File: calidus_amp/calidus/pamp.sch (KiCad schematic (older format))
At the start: 50 parts, among them U6 TDA7293, U7 TDA7293

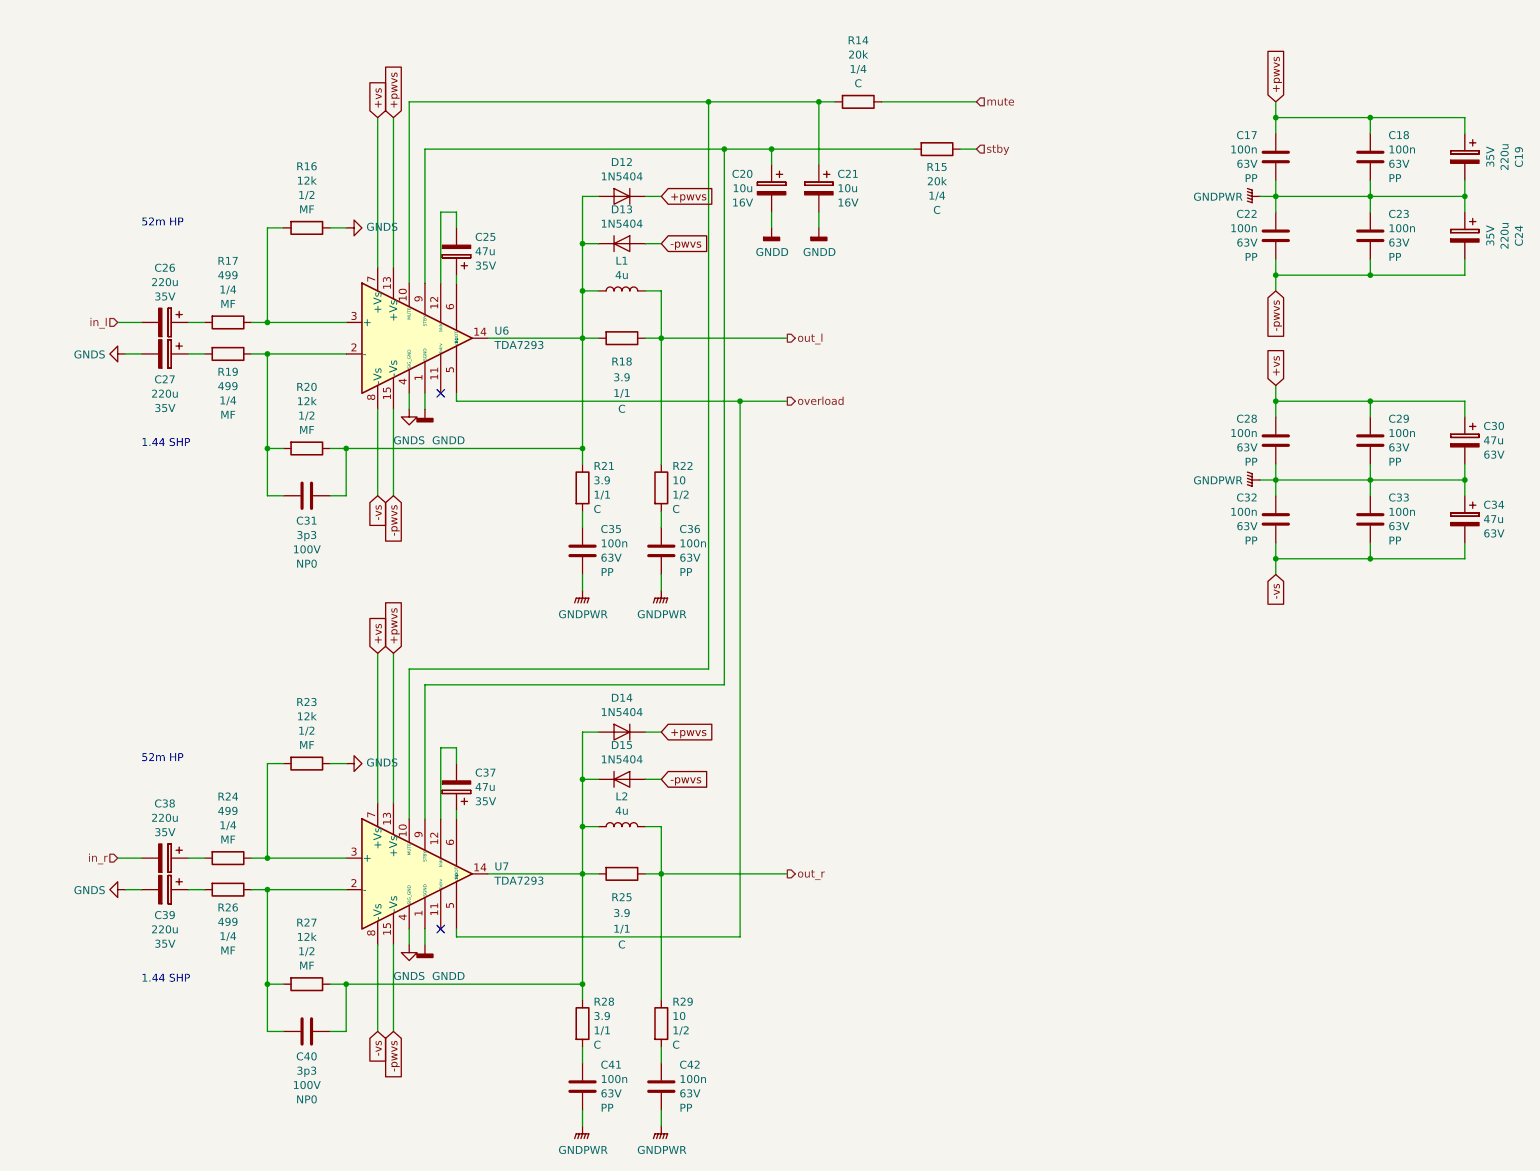
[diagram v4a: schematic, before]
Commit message: Updated schematic and footprinted Rybicon capacitors
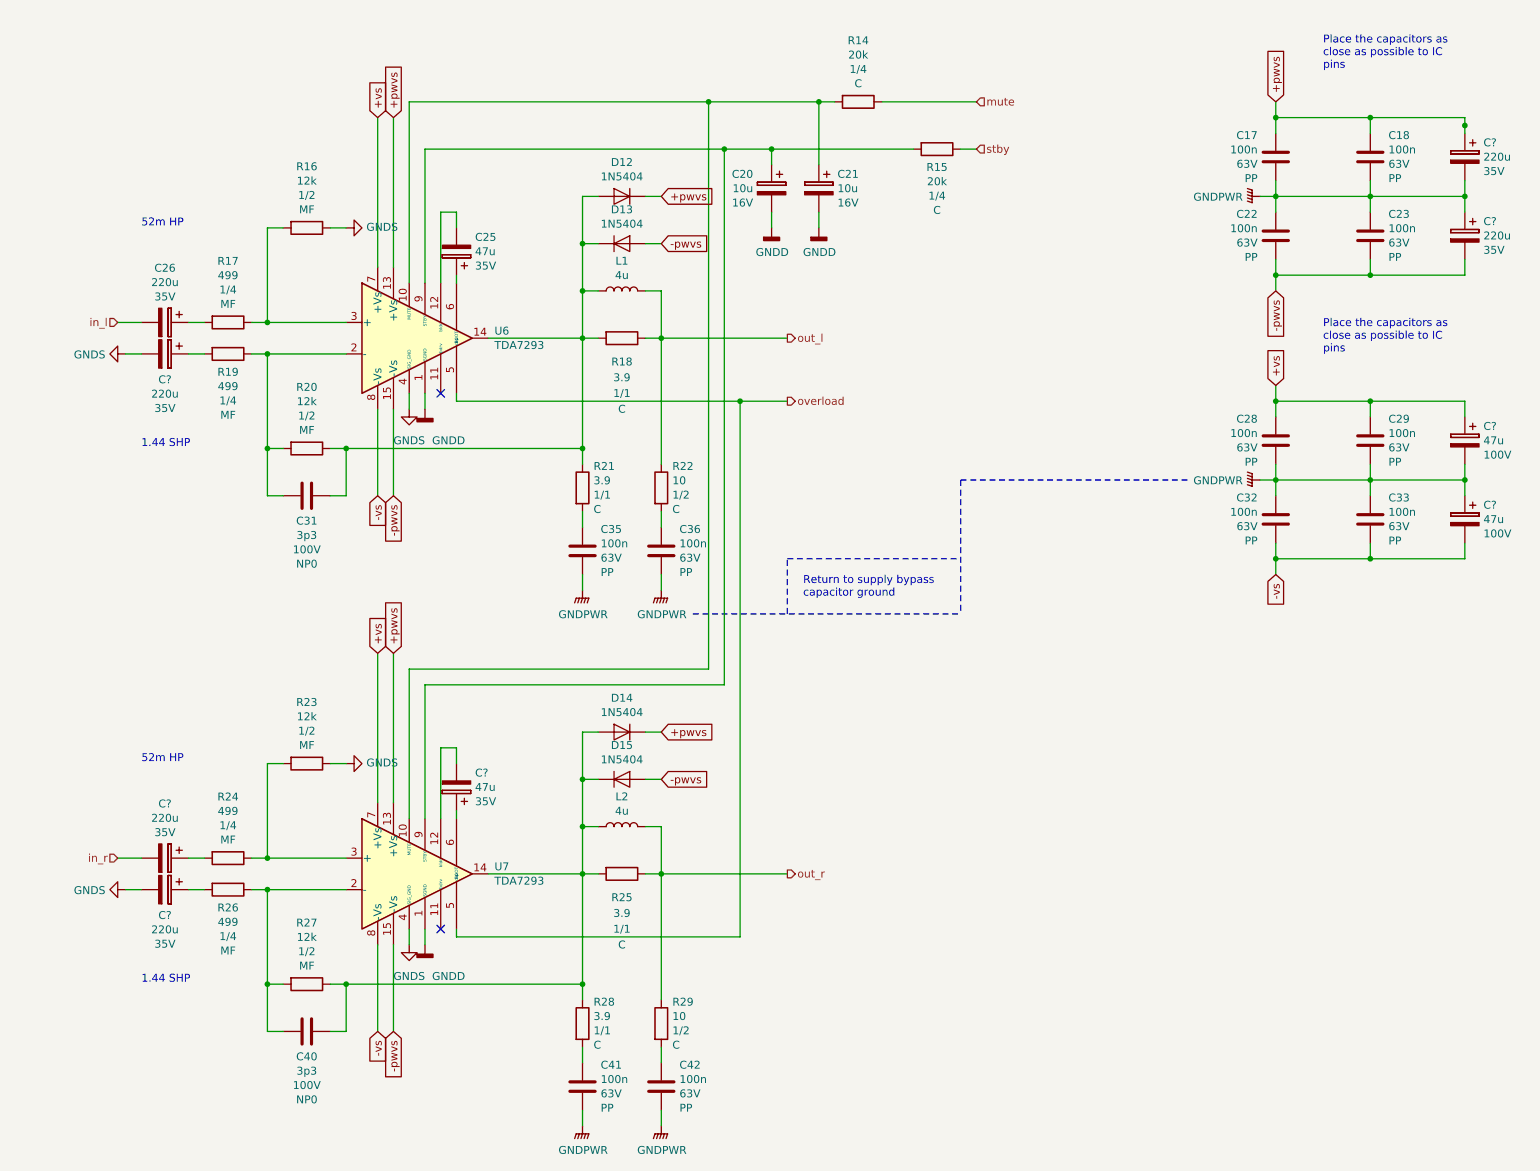
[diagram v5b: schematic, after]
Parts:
- removed C19, C24, C27, C38, C39: 220u, symbol Device:CP
- removed C30, C34, C37: 47u, symbol Device:CP
- added C?: 47u, Capacitor_THT:CP_Radial_D6.3mm_P2.50mm, symbol Device:CP
- added C? (x2): 47u, Capacitor_THT:CP_Radial_D10.0mm_P5.00mm, symbol Device:CP
- added C? (x5): 220u, Capacitor_THT:CP_Radial_D10.0mm_P5.00mm, symbol Device:CP
- C25: footprint (none) -> Capacitor_THT:CP_Radial_D6.3mm_P2.50mm; Manufacturer (none) -> Rybicon:35YXF47MEFC6.3X11; Supplier1 (none) -> Farnell:1144626
- C26: footprint (none) -> Capacitor_THT:CP_Radial_D10.0mm_P5.00mm; Manufacturer (none) -> Rybicon:35YXF220MEFC10X12.5; Supplier1 (none) -> Farnel:1144628
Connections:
- net +pwvs: now also C?.1
- net +vs: now also C?.1
- net -pwvs: now also C?.2
- net -vs: now also C?.2
- net GNDPWR: now also C?.1, C?.1, C?.2, C?.2
- net GNDS: now also C?.2, C?.2
- net in_r: now also C?.2
- net at U7.12 (bldr): now also C?.2
- net at U7.6 (BOOT): now also C?.1
- net at R19.2: now also C?.1
- net at R26.2: now also C?.1
- net at R24.2: now also C?.1
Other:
- note added: "Place the capacitors as\nclose as possible to IC\npins"
- note added: "Return to supply bypass \ncapacitor ground"
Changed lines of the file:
@@
 F 0 "C26" V 1905 2400 50  0000 C CNN
 F 1 "220u" V 1996 2400 50  0000 C CNN
-F 2 "" H 2288 2250 50  0001 C CNN
-F 3 "~" H 2250 2400 50  0001 C CNN
+F 2 "Capacitor_THT:CP_Radial_D10.0mm_P5.00mm" H 2288 2250 50  0001 C CNN
+F 3 "http://www.farnell.com/datasheets/2321304.pdf" H 2250 2400 50  0001 C CNN
 F 4 "35V" V 2087 2400 50  0000 C CNN "Voltage"
+F 5 "Rybicon:35YXF220MEFC10X12.5" V 2250 2400 50  0001 C CNN "Manufacturer"
+F 6 "Farnel:1144628" V 2250 2400 50  0001 C CNN "Supplier1"
 	1    2250 2400
 	0    1    1    0
@@
 F 0 "C25" H 3982 1859 50  0000 R CNN
 F 1 "47u" H 3982 1950 50  0000 R CNN
-F 2 "" H 4138 1800 50  0001 C CNN
-F 3 "~" H 4100 1950 50  0001 C CNN
+F 2 "Capacitor_THT:CP_Radial_D6.3mm_P2.50mm" H 4138 1800 50  0001 C CNN
+F 3 "http://www.farnell.com/datasheets/2321304.pdf" H 4100 1950 50  0001 C CNN
 F 4 "35V" H 3982 2041 50  0000 R CNN "Voltage"
+F 5 "Rybicon:35YXF47MEFC6.3X11" H 4100 1950 50  0001 C CNN "Manufacturer"
+F 6 "Farnell:1144626" H 4100 1950 50  0001 C CNN "Supplier1"
 	1    4100 1950
 	-1   0    0    1
@@
 $EndComp
 $Comp
-L Device:CP C27
-U 1 1 5C4684D2
-P 2250 2600
-F 0 "C27" V 2413 2600 50  0000 C CNN
-F 1 "220u" V 2504 2600 50  0000 C CNN
-F 2 "" H 2288 2450 50  0001 C CNN
-F 3 "~" H 2250 2600 50  0001 C CNN
-F 4 "35V" V 2595 2600 50  0000 C CNN "Voltage"
-	1    2250 2600
-	0    1    1    0
-$EndComp
-$Comp
-L Device:CP C39
-U 1 1 5C468E95
-P 2250 6000
-F 0 "C39" V 2413 6000 50  0000 C CNN
-F 1 "220u" V 2504 6000 50  0000 C CNN
-F 2 "" H 2288 5850 50  0001 C CNN
-F 3 "~" H 2250 6000 50  0001 C CNN
-F 4 "35V" V 2595 6000 50  0000 C CNN "Voltage"
-	1    2250 6000
-	0    1    1    0
-$EndComp
-$Comp
-L Device:CP C38
-U 1 1 5C468F39
-P 2250 5800
-F 0 "C38" V 1905 5800 50  0000 C CNN
-F 1 "220u" V 1996 5800 50  0000 C CNN
-F 2 "" H 2288 5650 50  0001 C CNN
-F 3 "~" H 2250 5800 50  0001 C CNN
-F 4 "35V" V 2087 5800 50  0000 C CNN "Voltage"
-	1    2250 5800
-	0    1    1    0
-$EndComp
-$Comp
 L Device:R R16
 U 1 1 5C469739
@@
 $EndComp
 $Comp
-L Device:CP C37
-U 1 1 5C469AA7
-P 4100 5350
-F 0 "C37" H 3982 5259 50  0000 R CNN
-F 1 "47u" H 3982 5350 50  0000 R CNN
-F 2 "" H 4138 5200 50  0001 C CNN
-F 3 "~" H 4100 5350 50  0001 C CNN
-F 4 "35V" H 3982 5441 50  0000 R CNN "Voltage"
-	1    4100 5350
-	-1   0    0    1
-$EndComp
-$Comp
 L Device:CP C21
 U 1 1 5C46A2D8
@@
 Wire Wire Line
 	9200 1600 9300 1600
-$Comp
-L Device:CP C19
-U 1 1 5C5797F2
-P 10500 1350
-F 0 "C19" V 10155 1350 50  0000 C CNN
-F 1 "220u" V 10246 1350 50  0000 C CNN
-F 2 "" H 10538 1200 50  0001 C CNN
-F 3 "~" H 10500 1350 50  0001 C CNN
-F 4 "35V" V 10337 1350 50  0000 C CNN "Voltage"
-	1    10500 1350
-	-1   0    0    -1
-$EndComp
-Wire Wire Line
-	10500 1200 10500 1100
+Wire Wire Line
+	10500 1200 10500 1150
 Wire Wire Line
 	9300 1100 9900 1100
@@
 Connection ~ 9900 2100
 Connection ~ 10500 1600
-$Comp
-L Device:CP C24
-U 1 1 5C59B1CB
-P 10500 1850
-F 0 "C24" V 10155 1850 50  0000 C CNN
-F 1 "220u" V 10246 1850 50  0000 C CNN
-F 2 "" H 10538 1700 50  0001 C CNN
-F 3 "~" H 10500 1850 50  0001 C CNN
-F 4 "35V" V 10337 1850 50  0000 C CNN "Voltage"
-	1    10500 1850
-	-1   0    0    -1
-$EndComp
 Wire Wire Line
 	10500 1700 10500 1600
@@
 Wire Wire Line
 	10500 3400 10500 3500
-$Comp
-L Device:CP C30
-U 1 1 5C5BB293
+Wire Wire Line
+	10500 3300 10500 3400
+Wire Wire Line
+	10500 3800 10500 3900
+Text Notes 6300 4150 0    50   ~ 0
+Return to supply bypass \ncapacitor ground
+Wire Notes Line
+	6200 3900 7300 3900
+Wire Notes Line
+	6200 4250 6200 3900
+Wire Notes Line
+	5600 4250 7300 4250
+Wire Notes Line
+	7300 3400 8750 3400
+Wire Notes Line
+	7300 3400 7300 4250
+Text Notes 9600 800  0    50   ~ 0
+Place the capacitors as\nclose as possible to IC\npins
+Text Notes 9600 2600 0    50   ~ 0
+Place the capacitors as\nclose as possible to IC\npins
+$Comp
+L Device:CP C?
+U 1 1 5C5AF4B7
+P 4100 5350
+F 0 "C?" H 3982 5259 50  0000 R CNN
+F 1 "47u" H 3982 5350 50  0000 R CNN
+F 2 "Capacitor_THT:CP_Radial_D6.3mm_P2.50mm" H 4138 5200 50  0001 C CNN
+F 3 "http://www.farnell.com/datasheets/2321304.pdf" H 4100 5350 50  0001 C CNN
+F 4 "35V" H 3982 5441 50  0000 R CNN "Voltage"
+F 5 "Rybicon:35YXF47MEFC6.3X11" H 4100 5350 50  0001 C CNN "Manufacturer"
+F 6 "Farnell:1144626" H 4100 5350 50  0001 C CNN "Supplier1"
+	1    4100 5350
+	-1   0    0    1
+$EndComp
+$Comp
+L Device:CP C?
+U 1 1 5C5B3FFC
 P 10500 3150
-F 0 "C30" H 10382 3241 50  0000 R CNN
+AR Path="/5C37BC48/5C5B3FFC" Ref="C?"  Part="1"
+AR Path="/5C37BC7C/5C5B3FFC" Ref="C?"  Part="1"
+F 0 "C?" H 10382 3241 50  0000 R CNN
 F 1 "47u" H 10382 3150 50  0000 R CNN
-F 2 "" H 10538 3000 50  0001 C CNN
-F 3 "~" H 10500 3150 50  0001 C CNN
-F 4 "63V" H 10382 3059 50  0000 R CNN "Voltage"
+F 2 "Capacitor_THT:CP_Radial_D10.0mm_P5.00mm" H 10538 3000 50  0001 C CNN
+F 3 "http://www.farnell.com/datasheets/2124421.pdf" H 10500 3150 50  0001 C CNN
+F 4 "100V" H 10382 3059 50  0000 R CNN "Voltage"
+F 5 "Rybicon:100YXF47MEFC10X16" H 10500 3150 50  0001 C CNN "Manufacturer"
+F 6 "Farnell:1144641" H 10500 3150 50  0001 C CNN "Supplier1"
 	1    10500 3150
 	-1   0    0    -1
 $EndComp
-Wire Wire Line
-	10500 3300 10500 3400
-$Comp
-L Device:CP C34
-U 1 1 5C5BB63A
+$Comp
+L Device:CP C?
+U 1 1 5C5CD581
 P 10500 3650
-F 0 "C34" H 10382 3741 50  0000 R CNN
+AR Path="/5C37BC48/5C5CD581" Ref="C?"  Part="1"
+AR Path="/5C37BC7C/5C5CD581" Ref="C?"  Part="1"
+F 0 "C?" H 10382 3741 50  0000 R CNN
 F 1 "47u" H 10382 3650 50  0000 R CNN
-F 2 "" H 10538 3500 50  0001 C CNN
-F 3 "~" H 10500 3650 50  0001 C CNN
-F 4 "63V" H 10382 3559 50  0000 R CNN "Voltage"
+F 2 "Capacitor_THT:CP_Radial_D10.0mm_P5.00mm" H 10538 3500 50  0001 C CNN
+F 3 "http://www.farnell.com/datasheets/2124421.pdf" H 10500 3650 50  0001 C CNN
+F 4 "100V" H 10382 3559 50  0000 R CNN "Voltage"
+F 5 "Rybicon:100YXF47MEFC10X16" H 10500 3650 50  0001 C CNN "Manufacturer"
+F 6 "Farnell:1144641" H 10500 3650 50  0001 C CNN "Supplier1"
 	1    10500 3650
 	-1   0    0    -1
 $EndComp
-Wire Wire Line
-	10500 3800 10500 3900
+$Comp
+L Device:CP C?
+U 1 1 5C5E5E74
+P 2250 2600
+F 0 "C?" V 2413 2600 50  0000 C CNN
+F 1 "220u" V 2504 2600 50  0000 C CNN
+F 2 "Capacitor_THT:CP_Radial_D10.0mm_P5.00mm" H 2288 2450 50  0001 C CNN
+F 3 "http://www.farnell.com/datasheets/2321304.pdf" H 2250 2600 50  0001 C CNN
+F 4 "35V" V 2595 2600 50  0000 C CNN "Voltage"
+F 5 "Rybicon:35YXF220MEFC10X12.5" V 2250 2600 50  0001 C CNN "Manufacturer"
+F 6 "Farnel:1144628" V 2250 2600 50  0001 C CNN "Supplier1"
+	1    2250 2600
+	0    1    1    0
+$EndComp
+$Comp
+L Device:CP C?
+U 1 1 5C5E631C
+P 2250 5800
+F 0 "C?" V 1905 5800 50  0000 C CNN
+F 1 "220u" V 1996 5800 50  0000 C CNN
+F 2 "Capacitor_THT:CP_Radial_D10.0mm_P5.00mm" H 2288 5650 50  0001 C CNN
+F 3 "http://www.farnell.com/datasheets/2321304.pdf" H 2250 5800 50  0001 C CNN
+F 4 "35V" V 2087 5800 50  0000 C CNN "Voltage"
+F 5 "Rybicon:35YXF220MEFC10X12.5" V 2250 5800 50  0001 C CNN "Manufacturer"
+F 6 "Farnel:1144628" V 2250 5800 50  0001 C CNN "Supplier1"
+	1    2250 5800
+	0    1    1    0
+$EndComp
+$Comp
+L Device:CP C?
+U 1 1 5C5E6449
+P 2250 6000
+F 0 "C?" V 2413 6000 50  0000 C CNN
+F 1 "220u" V 2504 6000 50  0000 C CNN
+F 2 "Capacitor_THT:CP_Radial_D10.0mm_P5.00mm" H 2288 5850 50  0001 C CNN
+F 3 "http://www.farnell.com/datasheets/2321304.pdf" H 2250 6000 50  0001 C CNN
+F 4 "35V" V 2595 6000 50  0000 C CNN "Voltage"
+F 5 "Rybicon:35YXF220MEFC10X12.5" V 2250 6000 50  0001 C CNN "Manufacturer"
+F 6 "Farnel:1144628" V 2250 6000 50  0001 C CNN "Supplier1"
+	1    2250 6000
+	0    1    1    0
+$EndComp
+$Comp
+L Device:CP C?
+U 1 1 5C5E6649
+P 10500 1350
+F 0 "C?" H 10382 1441 50  0000 R CNN
+F 1 "220u" H 10382 1350 50  0000 R CNN
+F 2 "Capacitor_THT:CP_Radial_D10.0mm_P5.00mm" H 10538 1200 50  0001 C CNN
+F 3 "http://www.farnell.com/datasheets/2321304.pdf" H 10500 1350 50  0001 C CNN
+F 4 "35V" H 10382 1259 50  0000 R CNN "Voltage"
+F 5 "Rybicon:35YXF220MEFC10X12.5" V 10500 1350 50  0001 C CNN "Manufacturer"
+F 6 "Farnel:1144628" V 10500 1350 50  0001 C CNN "Supplier1"
+	1    10500 1350
+	-1   0    0    -1
+$EndComp
+Connection ~ 10500 1150
+Wire Wire Line
+	10500 1150 10500 1100
+$Comp
+L Device:CP C?
+U 1 1 5C5E742F
+P 10500 1850
+F 0 "C?" H 10382 1941 50  0000 R CNN
+F 1 "220u" H 10382 1850 50  0000 R CNN
+F 2 "Capacitor_THT:CP_Radial_D10.0mm_P5.00mm" H 10538 1700 50  0001 C CNN
+F 3 "http://www.farnell.com/datasheets/2321304.pdf" H 10500 1850 50  0001 C CNN
+F 4 "35V" H 10382 1759 50  0000 R CNN "Voltage"
+F 5 "Rybicon:35YXF220MEFC10X12.5" V 10500 1850 50  0001 C CNN "Manufacturer"
+F 6 "Farnel:1144628" V 10500 1850 50  0001 C CNN "Supplier1"
+	1    10500 1850
+	-1   0    0    -1
+$EndComp
 $EndSCHEMATC

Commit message: Annotated the schematic
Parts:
- gave numbers to parts that had none: 8
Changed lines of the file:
@@
 Place the capacitors as\nclose as possible to IC\npins
 $Comp
-L Device:CP C?
+L Device:CP C37
 U 1 1 5C5AF4B7
 P 4100 5350
-F 0 "C?" H 3982 5259 50  0000 R CNN
+F 0 "C37" H 3982 5259 50  0000 R CNN
 F 1 "47u" H 3982 5350 50  0000 R CNN
 F 2 "Capacitor_THT:CP_Radial_D6.3mm_P2.50mm" H 4138 5200 50  0001 C CNN
@@
 P 10500 3150
 AR Path="/5C37BC48/5C5B3FFC" Ref="C?"  Part="1"
-AR Path="/5C37BC7C/5C5B3FFC" Ref="C?"  Part="1"
-F 0 "C?" H 10382 3241 50  0000 R CNN
+AR Path="/5C37BC7C/5C5B3FFC" Ref="C30"  Part="1"
+F 0 "C30" H 10382 3241 50  0000 R CNN
 F 1 "47u" H 10382 3150 50  0000 R CNN
 F 2 "Capacitor_THT:CP_Radial_D10.0mm_P5.00mm" H 10538 3000 50  0001 C CNN
@@
 P 10500 3650
 AR Path="/5C37BC48/5C5CD581" Ref="C?"  Part="1"
-AR Path="/5C37BC7C/5C5CD581" Ref="C?"  Part="1"
-F 0 "C?" H 10382 3741 50  0000 R CNN
+AR Path="/5C37BC7C/5C5CD581" Ref="C34"  Part="1"
+F 0 "C34" H 10382 3741 50  0000 R CNN
 F 1 "47u" H 10382 3650 50  0000 R CNN
 F 2 "Capacitor_THT:CP_Radial_D10.0mm_P5.00mm" H 10538 3500 50  0001 C CNN
@@
 $EndComp
 $Comp
-L Device:CP C?
+L Device:CP C27
 U 1 1 5C5E5E74
 P 2250 2600
-F 0 "C?" V 2413 2600 50  0000 C CNN
+F 0 "C27" V 2413 2600 50  0000 C CNN
 F 1 "220u" V 2504 2600 50  0000 C CNN
 F 2 "Capacitor_THT:CP_Radial_D10.0mm_P5.00mm" H 2288 2450 50  0001 C CNN
@@
 $EndComp
 $Comp
-L Device:CP C?
+L Device:CP C38
 U 1 1 5C5E631C
 P 2250 5800
-F 0 "C?" V 1905 5800 50  0000 C CNN
+F 0 "C38" V 1905 5800 50  0000 C CNN
 F 1 "220u" V 1996 5800 50  0000 C CNN
 F 2 "Capacitor_THT:CP_Radial_D10.0mm_P5.00mm" H 2288 5650 50  0001 C CNN
@@
 $EndComp
 $Comp
-L Device:CP C?
+L Device:CP C39
 U 1 1 5C5E6449
 P 2250 6000
-F 0 "C?" V 2413 6000 50  0000 C CNN
+F 0 "C39" V 2413 6000 50  0000 C CNN
 F 1 "220u" V 2504 6000 50  0000 C CNN
 F 2 "Capacitor_THT:CP_Radial_D10.0mm_P5.00mm" H 2288 5850 50  0001 C CNN
@@
 $EndComp
 $Comp
-L Device:CP C?
+L Device:CP C19
 U 1 1 5C5E6649
 P 10500 1350
-F 0 "C?" H 10382 1441 50  0000 R CNN
+F 0 "C19" H 10382 1441 50  0000 R CNN
 F 1 "220u" H 10382 1350 50  0000 R CNN
 F 2 "Capacitor_THT:CP_Radial_D10.0mm_P5.00mm" H 10538 1200 50  0001 C CNN
@@
 	10500 1150 10500 1100
 $Comp
-L Device:CP C?
+L Device:CP C24
 U 1 1 5C5E742F
 P 10500 1850
-F 0 "C?" H 10382 1941 50  0000 R CNN
+F 0 "C24" H 10382 1941 50  0000 R CNN
 F 1 "220u" H 10382 1850 50  0000 R CNN
 F 2 "Capacitor_THT:CP_Radial_D10.0mm_P5.00mm" H 10538 1700 50  0001 C CNN
